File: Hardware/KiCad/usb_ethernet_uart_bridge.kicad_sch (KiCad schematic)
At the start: 9 parts, among them U1 XR22801IL32TR-F, Y1 ABM8-25.000MHZ-B2-T3

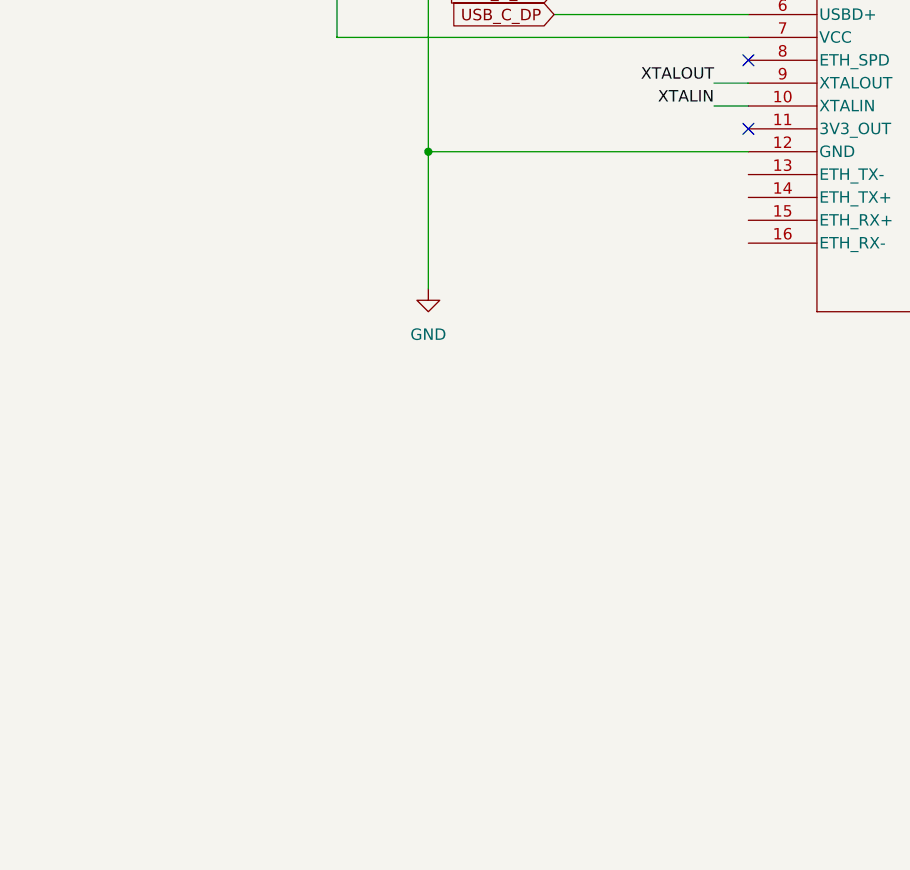
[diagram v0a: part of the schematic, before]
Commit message: USB_Bridge: add transformerless connection between usb bridge and SOM
- Ethernet: Add fourth rj45 jack
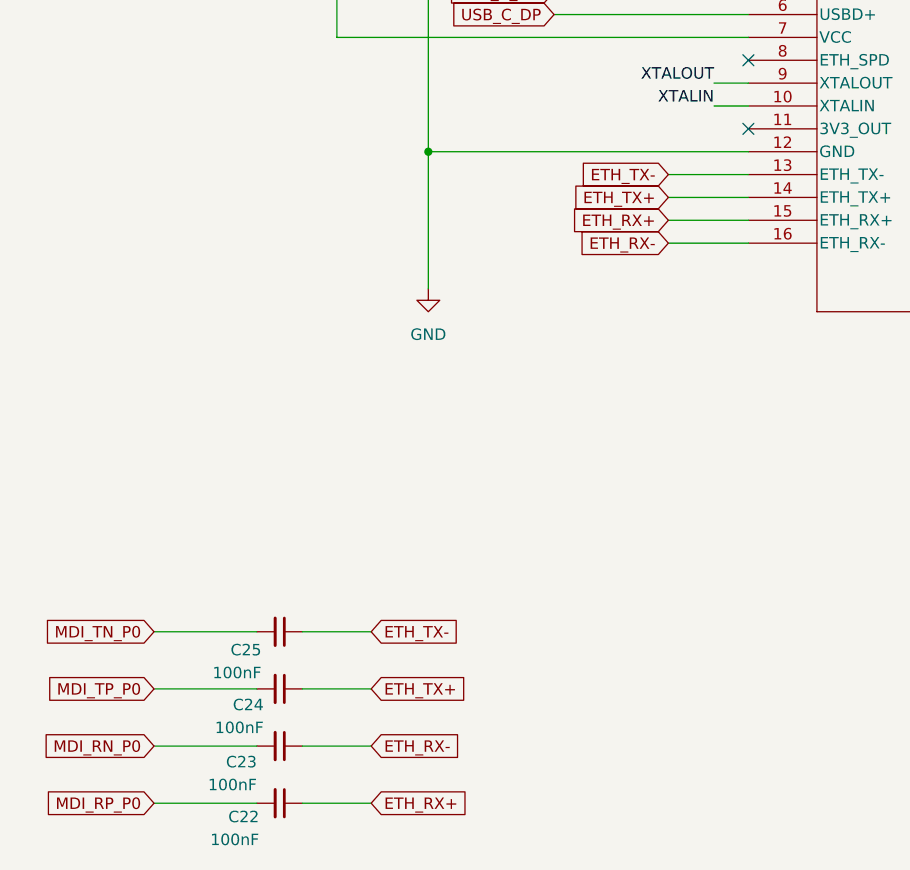
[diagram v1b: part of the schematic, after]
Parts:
- added C22, C23, C24, C25: 100nF, Capacitor_SMD:C_0603_1608Metric, symbol Device:C_Small
- U1: footprint footprints:QFN-32 -> Package_DFN_QFN:QFN-32-1EP_5x5mm_P0.5mm_EP3.65x3.65mm
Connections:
- net ETH_TX-: now reaches U1.13 (ETH_TX-)
- net ETH_TX-: now also C25.1
- net ETH_TX+: now reaches U1.14 (ETH_TX+)
- net ETH_TX+: now also C24.1
- net ETH_RX+: now reaches U1.15 (ETH_RX+)
- net ETH_RX+: now also C22.1
- net ETH_RX-: now reaches U1.16 (ETH_RX-)
- net ETH_RX-: now also C23.1
- new net MDI_RN_P0: C23.2
- new net MDI_RP_P0: C22.2
- new net MDI_TN_P0: C25.2
- new net MDI_TP_P0: C24.2
